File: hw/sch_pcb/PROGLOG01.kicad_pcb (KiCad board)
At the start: 2 copper layers, 60.5 x 40.1 mm, 66 parts, among them J1 JUMP_3X2, J10 HEADER_2x01_PARALLEL, J11 HEADER_2x01_PARALLEL, J13 HEADER_2x01_PARALLEL, J14 HEADER_2x01_PARALLEL, J15 HEADER_2x01_PARALLEL, J16 HEADER_2x01_PARALLEL, J17 HEADER_2x01_PARALLEL, J18 HEADER_2x01_PARALLEL, J19 HEADER_2x01_PARALLEL, J2 HEADER_2x01, J20 HEADER_2x01_PARALLEL, J21 HEADER_2x01_PARALLEL, J22 HEADER_2x01_PARALLEL, J23 HEADER_2x01_PARALLEL, J24 HEADER_2x01_PARALLEL, J25 HEADER_2x01_PARALLEL, J26 SATA, J27 HEADER_2x01_PARALLEL, J28 HEADER_2x01_PARALLEL, J29 HEADER_2x01_PARALLEL, J3 HEADER_2x02_PARALLEL, J30 HEADER_2x01_PARALLEL, J31 HEADER_2x01_PARALLEL, J32 HEADER_2x01_PARALLEL, J33 HEADER_2x01_PARALLEL, J34 HEADER_2x01_PARALLEL, J4 HEADER_2x04, J5 HEADER_2x01_PARALLEL, J6 HEADER_2x01_PARALLEL, J7 HEADER_2x01_PARALLEL, J8 HEADER_2x01_PARALLEL, J9 HEADER_2x01_PARALLEL, M1 HOLE, M2 HOLE, M3 HOLE, M4 HOLE, SW1 SW_Push, U1 TPS22919DCK, U2 MIC5504-1.2YM5, U3 AT25SF081-SSHD-X, U4 ICE40UP5K-SG48ITR, X1 ISM92-3351AH24.00

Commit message: Update project and documentation.
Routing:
- net /RGB1: track 44.4 -> 43.7 mm
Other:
- board text added: "0A"
- board text added: "13B"
- board text added: "16A"
- board text added: "18A"
- board text added: "20A"
- board text added: "22B"
- board text added: "23B"
- board text added: "24A"
- board text added: "29B"
- board text added: "2A"
- board text added: "31B"
- board text added: "37A 36B 39A 38B"
- board text added: "41A"
- board text added: "42B"
- board text added: "43A"
- board text added: "44B"
- board text added: "48B"
- board text added: "49A"
- board text added: "4A"
- board text added: "50B"
- board text added: "51A"
- board text added: "5B"
- board text added: "6A"
- board text added: "8A"
- board text added: "9B"
- board text added: "G0/46B"
- board text added: "G1/45A"
- board text added: "G6/3B"
- board text added: "PROGLOG01B MLAB.cz"
- board text added: "povik,kaklik 2023"
- board text removed: "0a"
- board text removed: "13b"
- board text removed: "16a"
- board text removed: "18a"
- board text removed: "20a"
- board text removed: "22b"
- board text removed: "23b"
- board text removed: "24a"
- board text removed: "29b"
- board text removed: "2a"
- board text removed: "31b"
- board text removed: "37a 36b 39a 38b"
- board text removed: "41a"
- board text removed: "42b"
- board text removed: "43a"
- board text removed: "44b"
- board text removed: "48b"
- board text removed: "49a"
- board text removed: "4a"
- board text removed: "50b"
- board text removed: "51a"
- board text removed: "5b"
- board text removed: "6a"
- board text removed: "8a"
- board text removed: "9b"
- board text removed: "G0/46b"
- board text removed: "G1/45a"
- board text removed: "G6/3b"
- board text removed: "PROGLOG01A MLAB.CZ"
- board text removed: "povik 2019"

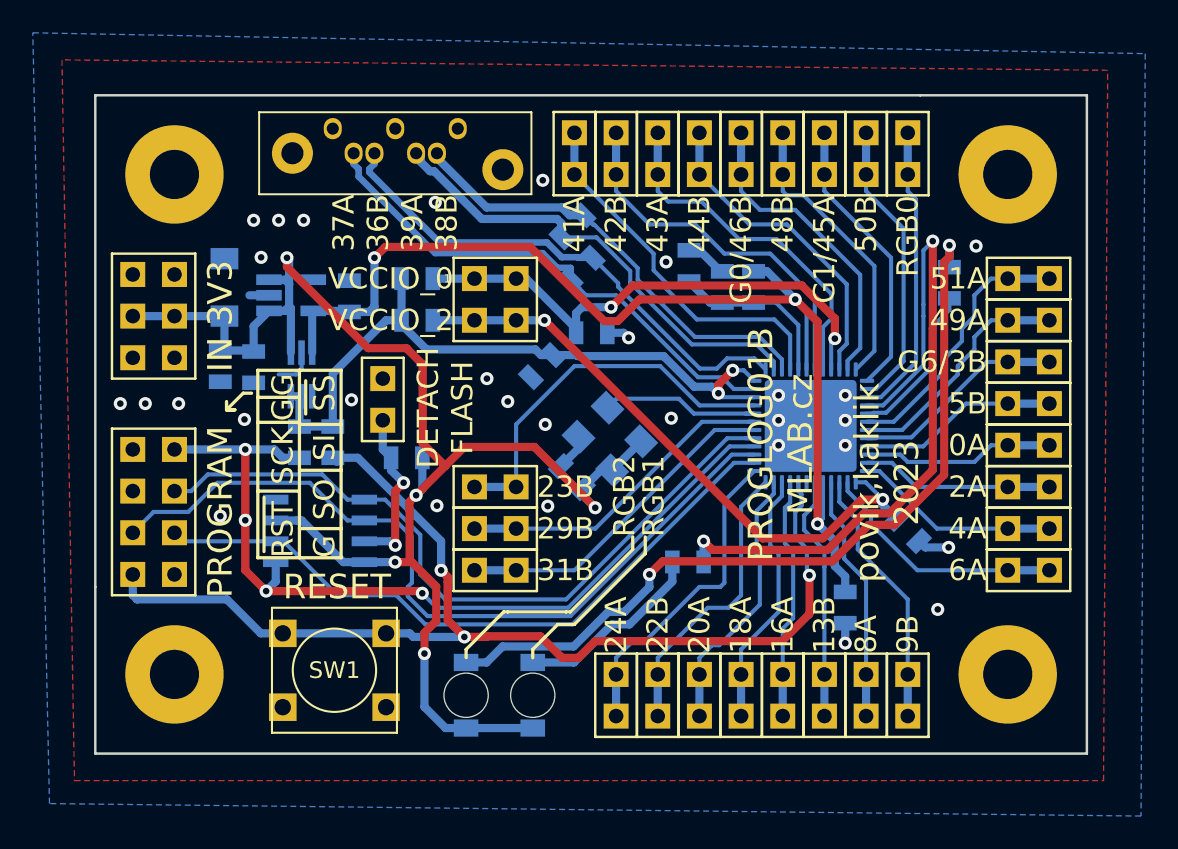
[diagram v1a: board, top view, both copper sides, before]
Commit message: Fix unconnected tracks DRC errors.
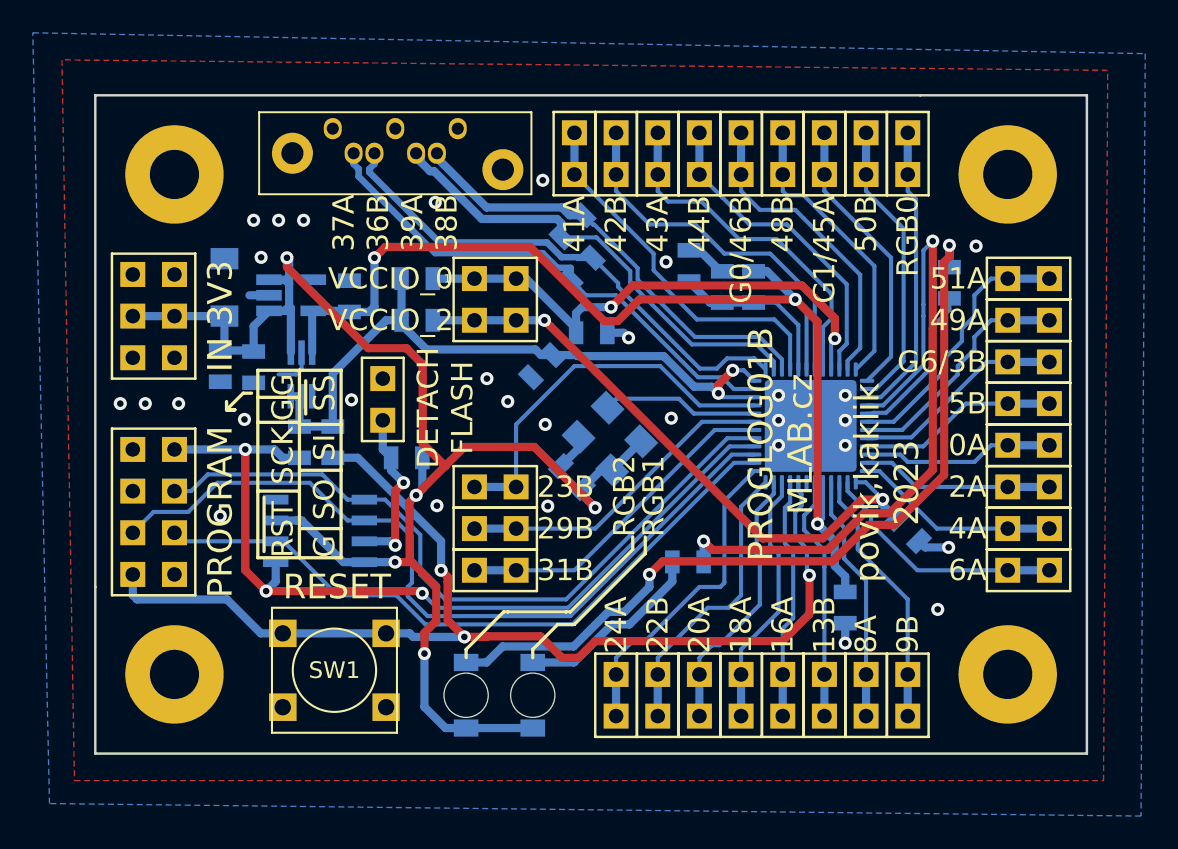
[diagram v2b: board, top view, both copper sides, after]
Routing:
- net /SPI_SI: track 45.4 -> 44.4 mm
- net /IOB_16a: track 15.5 -> 14.9 mm
- net /IOT_51a: track 16.9 -> 16.4 mm
- net /IOB_25b: track 10.1 -> 9.55 mm
- net /SPI_SS: vias 4 -> 3
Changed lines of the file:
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@@
   (via (at 168.656 109.22) (size 0.8) (drill 0.4) (layers "F.Cu" "B.Cu") (net 2))
   (via (at 170.18 109.22) (size 0.8) (drill 0.4) (layers "F.Cu" "B.Cu") (net 2))
-  (segment (start 195.707 112.3315) (end 195.2625 112.3315) (width 0.5) (layer "B.Cu") (net 2))
   (segment (start 189.6872 116.078) (end 189.992 116.3828) (width 0.5) (layer "B.Cu") (net 2))
   (segment (start 170.053 117.288) (end 170.053 118.288) (width 0.25) (layer "B.Cu") (net 2))
@@
   (segment (start 170.768 114.742) (end 172.908 114.742) (width 0.5) (layer "B.Cu") (net 3))
   (segment (start 201.513459 127.72646) (end 202.56149 128.774491) (width 0.5) (layer "B.Cu") (net 3))
-  (segment (start 170.768 114.742) (end 171.223 114.742) (width 0.5) (layer "B.Cu") (net 3))
   (segment (start 200.8418 118.3174) (end 200.8418 114.7358) (width 0.25) (layer "B.Cu") (net 3))
   (segment (start 174.1725 114.808) (end 172.974 114.808) (width 0.5) (layer "B.Cu") (net 3))
@@
   (segment (start 176.641466 134.402) (end 175.2096 134.402) (width 0.5) (layer "B.Cu") (net 11))
   (segment (start 200.8632 130.709621) (end 201.0156 130.862021) (width 0.25) (layer "B.Cu") (net 11))
-  (segment (start 172.212 123.952) (end 171.958 123.698) (width 0.5) (layer "B.Cu") (net 11))
   (segment (start 200.3418 125.7299) (end 200.533 125.9211) (width 0.25) (layer "B.Cu") (net 11))
   (segment (start 200.533 126.619) (end 200.152 127) (width 0.25) (layer "B.Cu") (net 11))
@@
   (segment (start 161.036 127) (end 159.766 128.27) (width 0.25) (layer "B.Cu") (net 13))
   (segment (start 173.88076 127.5207) (end 172.85576 127.5207) (width 0.25) (layer "B.Cu") (net 13))
-  (segment (start 174.35576 127.5207) (end 173.88076 127.5207) (width 0.25) (layer "B.Cu") (net 13))
   (segment (start 175.7807 127.5207) (end 173.88076 127.5207) (width 0.25) (layer "B.Cu") (net 13))
   (segment (start 176.53 131.572) (end 176.784 131.318) (width 0.25) (layer "B.Cu") (net 13))
@@
   (segment (start 166.624 130.556) (end 166.624 123.19) (width 0.5) (layer "F.Cu") (net 14))
   (segment (start 167.894 131.826) (end 177.282694 131.826) (width 0.5) (layer "F.Cu") (net 14))
-  (via (at 166.624 127.508) (size 0.8) (drill 0.4) (layers "F.Cu" "B.Cu") (net 14))
   (via (at 166.624 123.19) (size 0.8) (drill 0.4) (layers "F.Cu" "B.Cu") (net 14))
   (via (at 167.894 131.826) (size 0.8) (drill 0.4) (layers "F.Cu" "B.Cu") (net 14))
@@
   (segment (start 197.6543 122.5049) (end 196.0111 122.5049) (width 0.25) (layer "B.Cu") (net 15))
   (segment (start 162.306 125.73) (end 163.318 125.73) (width 0.25) (layer "B.Cu") (net 15))
-  (segment (start 197.6543 122.5049) (end 197.1168 122.5049) (width 0.25) (layer "B.Cu") (net 15))
   (segment (start 164.334 124.714) (end 171.31906 124.714) (width 0.25) (layer "B.Cu") (net 15))
-  (segment (start 174.35576 126.2507) (end 173.88076 126.2507) (width 0.25) (layer "B.Cu") (net 15))
   (segment (start 172.85576 126.2507) (end 173.88076 126.2507) (width 0.25) (layer "B.Cu") (net 15))
   (segment (start 186.69 103.886) (end 186.69 106.426) (width 0.5) (layer "B.Cu") (net 16))
@@
   (segment (start 199.8418 116.225) (end 198.882 115.2652) (width 0.25) (layer "B.Cu") (net 16))
   (segment (start 194.1576 115.2652) (end 192.278 113.3856) (width 0.25) (layer "B.Cu") (net 16))
-  (segment (start 186.69 106.8324) (end 186.69 106.426) (width 0.25) (layer "B.Cu") (net 16))
-  (segment (start 197.866 114.2365) (end 197.612 114.2365) (width 0.25) (layer "B.Cu") (net 17))
   (segment (start 200.3418 115.6074) (end 198.9709 114.2365) (width 0.25) (layer "B.Cu") (net 17))
   (segment (start 198.9709 114.2365) (end 197.612 114.2365) (width 0.25) (layer "B.Cu") (net 17))
@@
   (segment (start 204.5293 121.5049) (end 206.1551 121.5049) (width 0.25) (layer "B.Cu") (net 29))
   (segment (start 211.074 113.796) (end 212.094 112.776) (width 0.25) (layer "B.Cu") (net 29))
-  (segment (start 204.5293 121.5049) (end 205.0668 121.5049) (width 0.25) (layer "B.Cu") (net 29))
   (segment (start 211.074 115.062) (end 211.074 113.796) (width 0.25) (layer "B.Cu") (net 29))
   (segment (start 212.094 112.776) (end 213.106 112.776) (width 0.25) (layer "B.Cu") (net 29))
@@
   (segment (start 200.696999 128.110001) (end 201.93 129.343002) (width 0.25) (layer "B.Cu") (net 39))
   (segment (start 201.93 130.359002) (end 201.93 136.906) (width 0.25) (layer "B.Cu") (net 39))
-  (segment (start 199.8418 136.4542) (end 199.39 136.906) (width 0.25) (layer "B.Cu") (net 40))
   (segment (start 199.39 136.906) (end 199.39 139.446) (width 0.5) (layer "B.Cu") (net 40))
   (segment (start 200.025 129.413) (end 200.025 133.477) (width 0.25) (layer "B.Cu") (net 40))
@@
   (segment (start 187.96 128.016) (end 194.4711 121.5049) (width 0.25) (layer "B.Cu") (net 46))
   (segment (start 194.4711 121.5049) (end 197.6543 121.5049) (width 0.25) (layer "B.Cu") (net 46))
-  (segment (start 197.6543 121.5049) (end 197.31628 121.5049) (width 0.25) (layer "B.Cu") (net 46))
   (segment (start 183.134 128.016) (end 187.96 128.016) (width 0.25) (layer "B.Cu") (net 46))
   (segment (start 193.059305 120.097805) (end 193.9664 121.0049) (width 0.25) (layer "B.Cu") (net 47))
-  (segment (start 197.1168 121.0049) (end 197.6543 121.0049) (width 0.25) (layer "B.Cu") (net 47))
   (segment (start 188.707579 120.645812) (end 189.255586 120.097805) (width 0.25) (layer "B.Cu") (net 47))
   (segment (start 193.9664 121.0049) (end 197.6543 121.0049) (width 0.25) (layer "B.Cu") (net 47))

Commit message: Fix #1 Layout improvement vias position improvement.
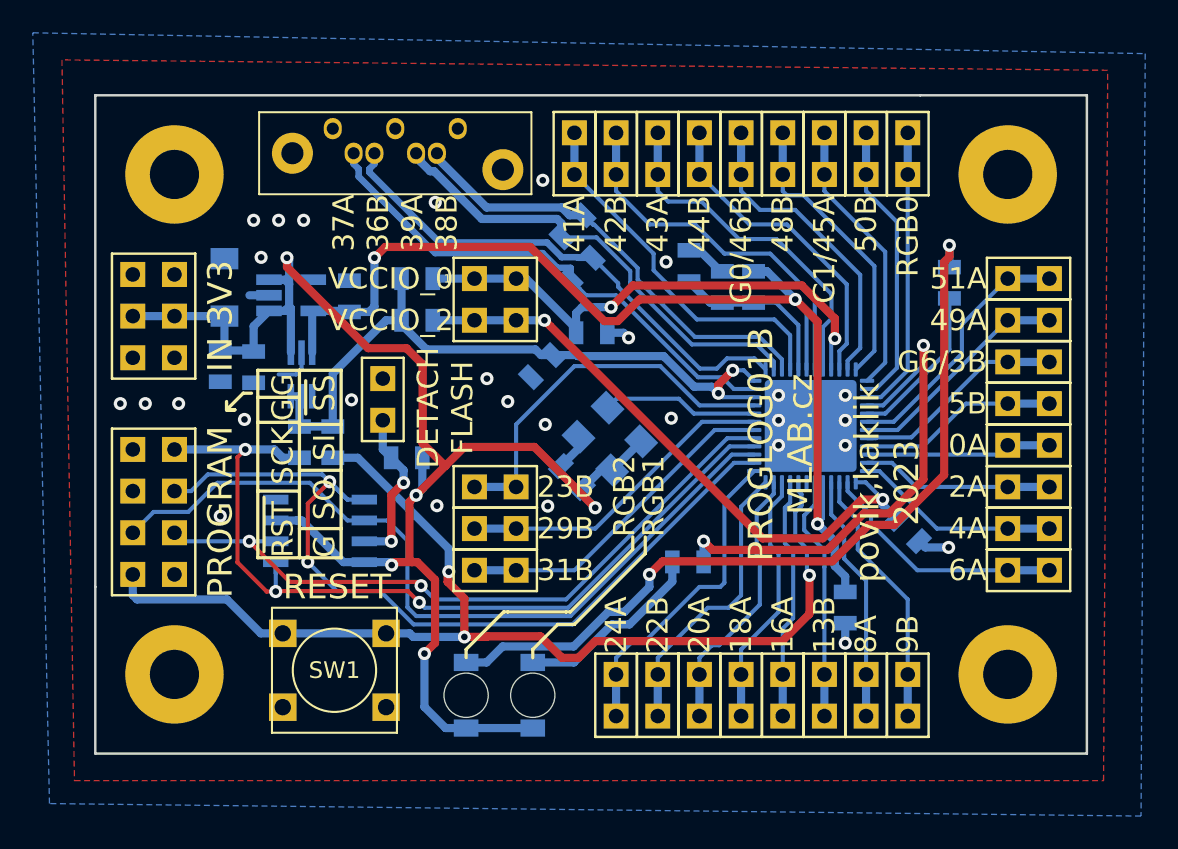
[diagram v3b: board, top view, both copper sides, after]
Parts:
- D1: value 0.0V -> BZV55C-5,6V
- D2: value LED -> YELLOW
- D3: value LED -> BLUE
- U3: value AT25SF081-SSHD-X -> AT25SF081-SSH
- U4: value ICE40UP5K-SG48ITR -> ICE40UP5K-SG48I
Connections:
- net /SATA_1N renamed /IOT_36b
- net /SATA_1P renamed /IOT_37a
- net /SATA_2N renamed /IOT_38b
- net /SATA_2P renamed /IOT_39a
- U2 pad 4: Net-(U2-Pad4) -> unconnected-(U2-Pad4)
- U4 pad 14: /SPI_SO -> /SPI_SI
- U4 pad 17: /SPI_SI -> /SPI_SO
- U4 pad 7: Net-(U4-Pad7) -> unconnected-(U4-Pad7)
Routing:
- net /RGB1: track 43.7 -> 30.5 mm
- net /SPI_SI: track 44.4 -> 52.5 mm, vias 0 -> 2
- net /SPI_SO: track 41.7 -> 42.7 mm, vias 0 -> 2
- net /IOT_49a: track 14.6 -> 13.9 mm
- net /IOT_51a: track 16.4 -> 15.8 mm
- net /SPI_SS: track 53.3 -> 53.8 mm
- net GND: vias 30 -> 28

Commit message: Imrove layout - avoid sharp edges.
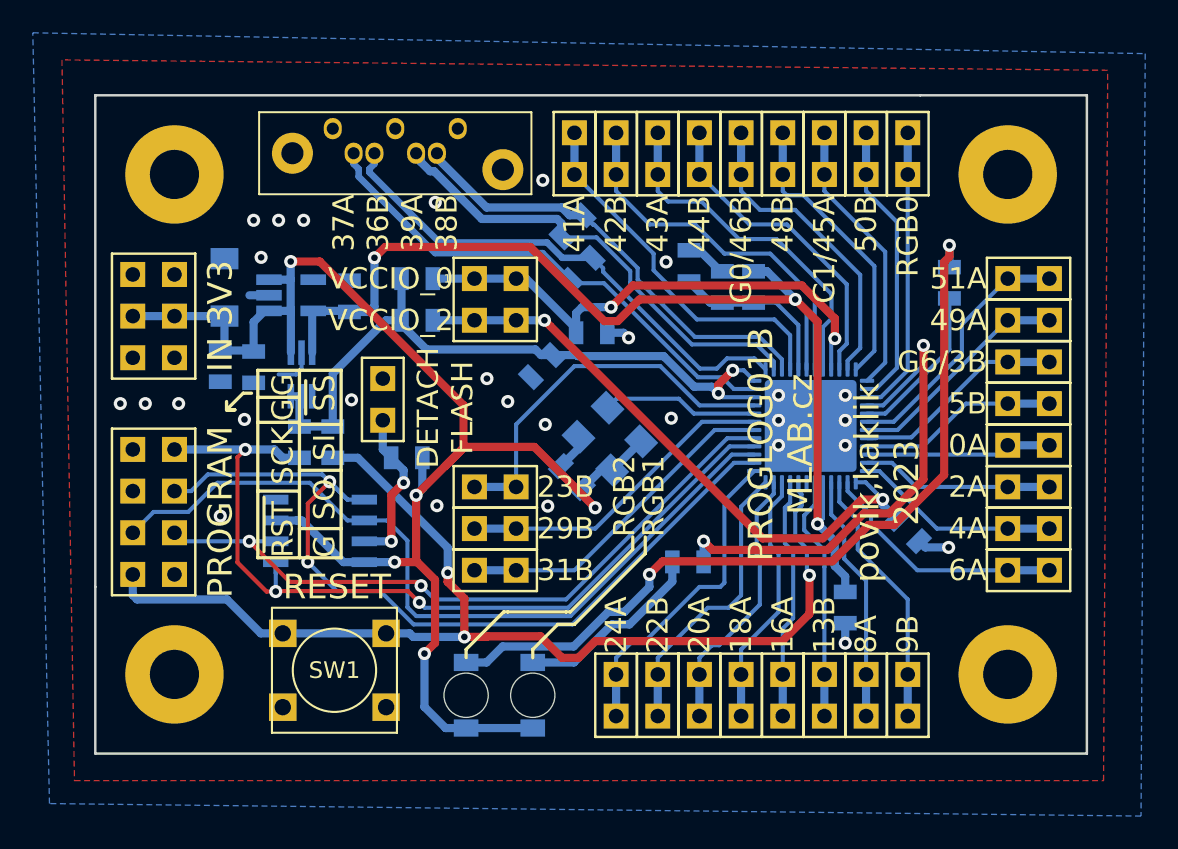
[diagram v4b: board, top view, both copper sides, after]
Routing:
- net /IOT_37a: track 32.4 -> 31.0 mm

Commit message: Update footprints from library. Improve bottom silkscreen.
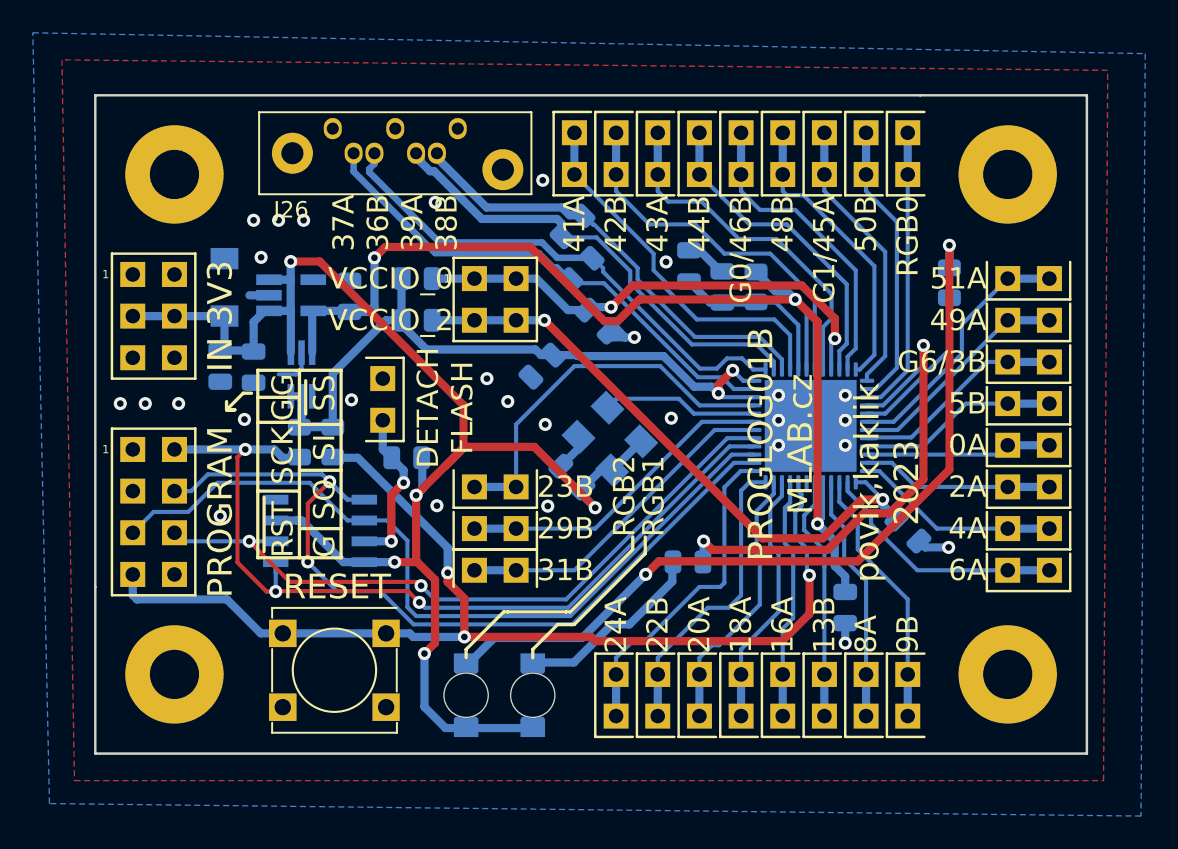
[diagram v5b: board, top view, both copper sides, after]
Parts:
- C1, C10, C2, C3, C4, C5, C6, C7, C8, C9: footprint Mlab_R:SMD-0805 -> Capacitor_SMD:C_0805_2012Metric
- R1, R10, R2, R3, R4, R5, R6, R7, R8, R9: footprint Mlab_R:SMD-0805 -> Resistor_SMD:R_0805_2012Metric
- moved C8 0.81 mm to (188.1, 115.4), turned to -45 degrees
- moved R4 0.15 mm to (197.8, 113.3)
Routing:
- net /VCCIO_0: track 32.0 -> 30.0 mm
- net /VCCIO_1: track 43.1 -> 44.8 mm
- net GND: track 13.1 -> 14.6 mm
- net /NRESET: track 69.0 -> 68.1 mm
- net /IOB_22b: track 17.7 -> 18.3 mm
